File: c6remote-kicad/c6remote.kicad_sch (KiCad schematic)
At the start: 23 parts, among them Q1 MMBT2222A, SW1 SW_Push, SW10 SW_Push, SW11 SW_Push, SW2 SW_Push, SW3 SW_Push, SW4 SW_Push, SW5 SW_Push, SW6 SW_Push, SW7 SW_Push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

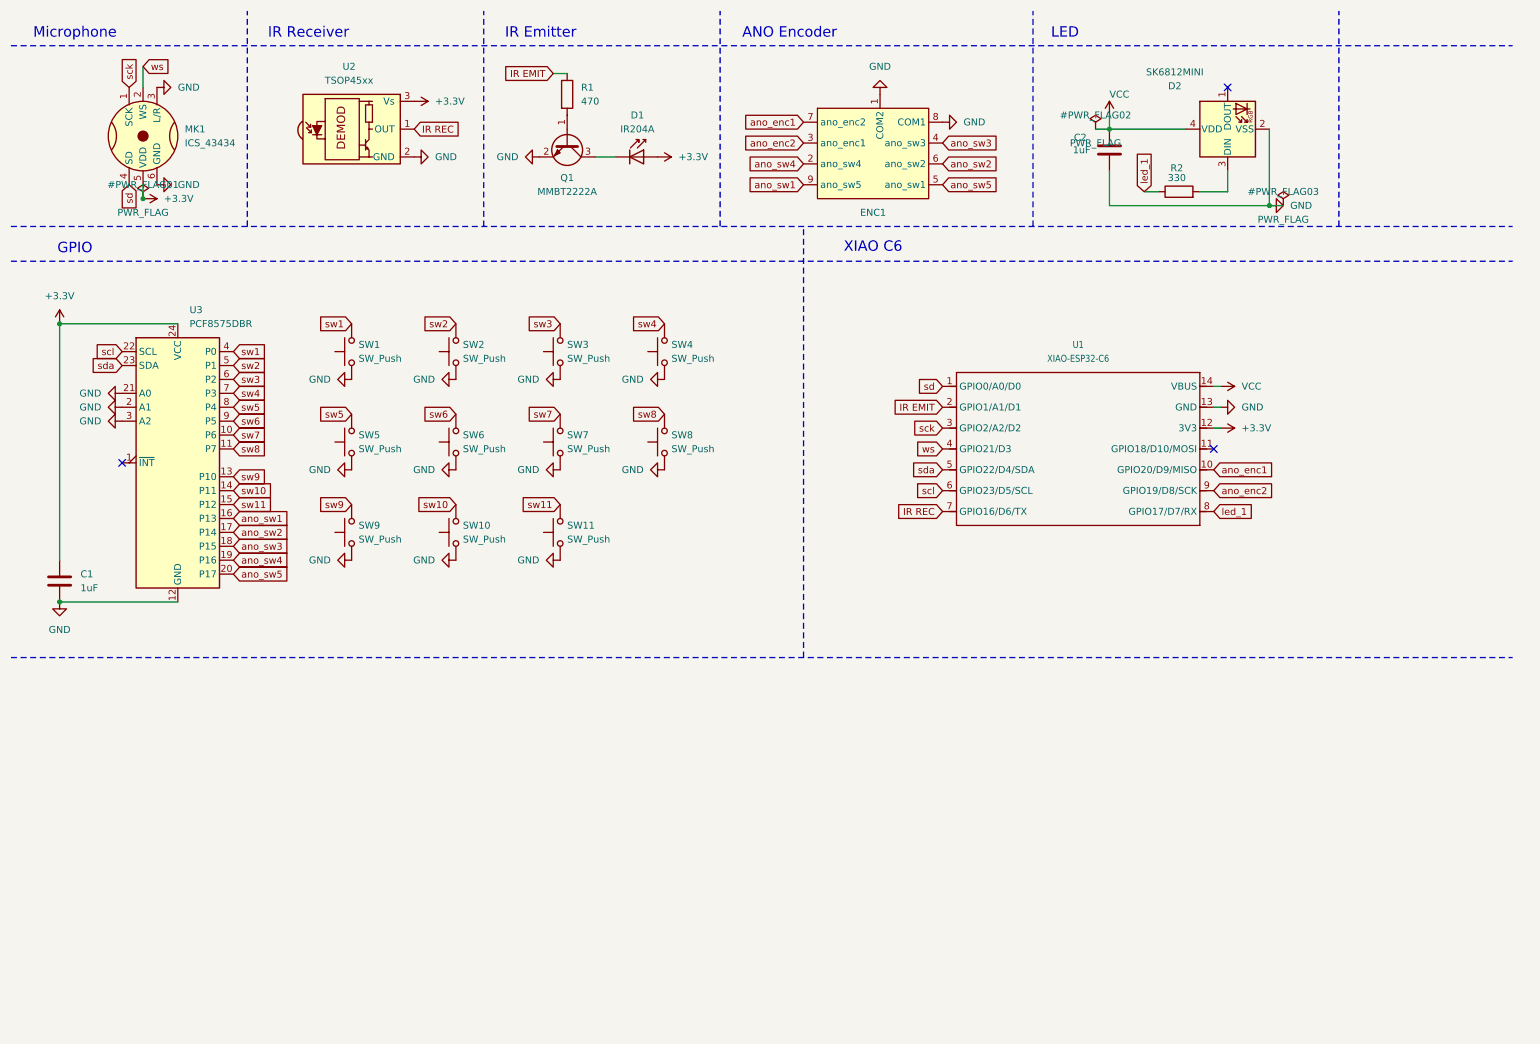
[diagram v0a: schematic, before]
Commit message: feat(kicad): update xiao c6 board
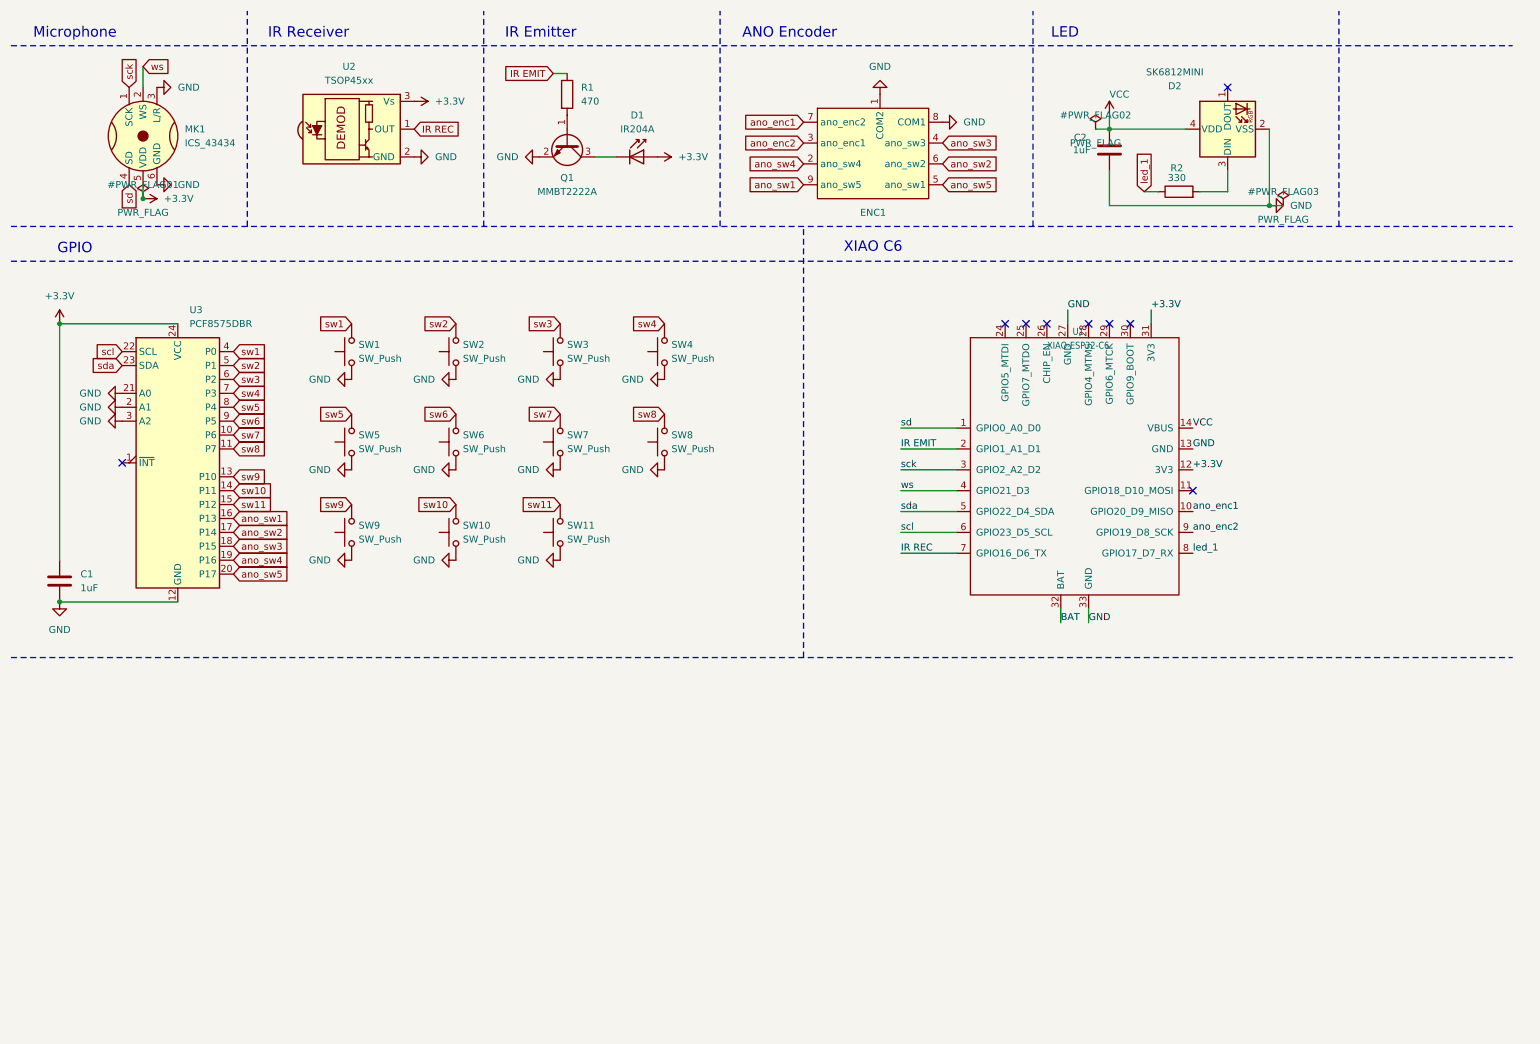
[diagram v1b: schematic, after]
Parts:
- U1: footprint Library:XIAO-ESP32C6-DIP -> Seeed_Studio_XIAO_Series:XIAO-ESP32-C6-SMD; symbol Seeed_Studio_XIAO_Series:XIAO_ESP32-C6-DIP -> Seeed_Studio_XIAO_Series:XIAO-ESP32-C6-SMD
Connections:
- net +3.3V: now also U1.31 (3V3)
- net GND: now also U1.27 (GND), U1.33 (GND)
- new net BAT: U1.32 (BAT)
- no-connect marks 3 -> 9

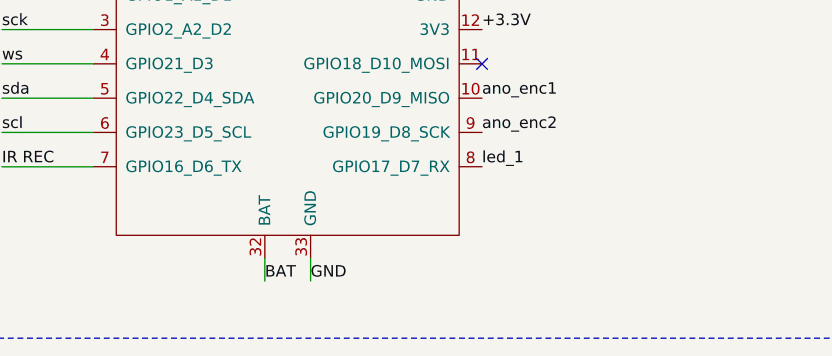
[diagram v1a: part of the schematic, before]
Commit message: fix(kicad): sync battery connector parity
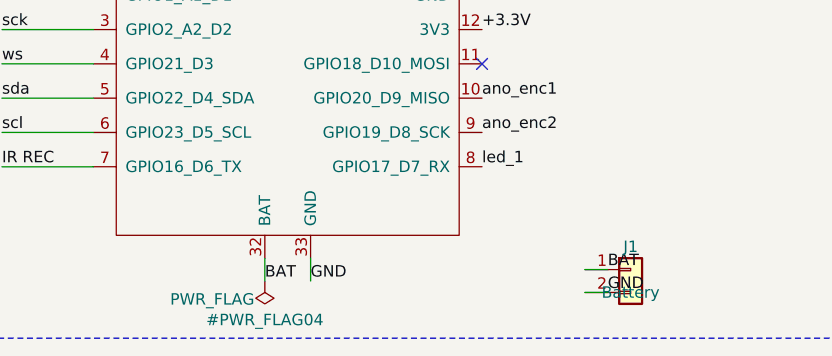
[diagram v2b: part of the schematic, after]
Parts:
- added J1: Battery, Local:WirePad_1x02_P2.54mm_Back, symbol Connector_Generic:Conn_01x02
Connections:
- net BAT: now also J1.1 (Pin_1)
- net GND: now also J1.2 (Pin_2)
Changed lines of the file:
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@@
 	(wire
 		(pts
-			(xy 203.2 120.65) (xy 203.2 123.19)
-		)
-		(stroke
-			(width 0)
-			(type default)
-		)
-	)
-	(wire
-		(pts
 			(xy 212.09 46.99) (xy 241.3 46.99)
 		)
@@
 		)
 	)
+	(wire
+		(pts
+			(xy 238.76 124.46) (xy 241.3 124.46)
+		)
+		(stroke
+			(width 0)
+			(type default)
+		)
+	)
+	(wire
+		(pts
+			(xy 203.2 123.19) (xy 203.2 120.65)
+		)
+		(stroke
+			(width 0)
+			(type default)
+		)
+	)
+	(wire
+		(pts
+			(xy 238.76 121.92) (xy 241.3 121.92)
+		)
+		(stroke
+			(width 0)
+			(type default)
+		)
+	)
 	(polyline
 		(pts
@@
 		)
 	)
-	(label "+3.3V"
-		(at 219.71 66.04 0)
+	(label "GND"
+		(at 241.3 124.46 0)
 		(effects
 			(font
@@
 		)
 	)
-	(label "GND"
-		(at 227.33 91.44 0)
+	(label "+3.3V"
+		(at 219.71 66.04 0)
 		(effects
 			(font
@@
 		)
 	)
-	(label "BAT"
-		(at 203.2 123.19 0)
+	(label "GND"
+		(at 227.33 91.44 0)
 		(effects
 			(font
@@
 		)
 	)
+	(label "BAT"
+		(at 241.3 121.92 0)
+		(effects
+			(font
+				(size 1.27 1.27)
+			)
+			(justify left bottom)
+		)
+	)
 	(label "+3.3V"
 		(at 227.33 95.25 0)
@@
 		)
 	)
+	(label "BAT"
+		(at 203.2 123.19 0)
+		(effects
+			(font
+				(size 1.27 1.27)
+			)
+			(justify left bottom)
+		)
+	)
 	(label "IR EMIT"
 		(at 173.99 91.44 0)
@@
 	)
 	(symbol
+		(lib_id "Connector_Generic:Conn_01x02")
+		(at 243.84 121.92 0)
+		(unit 1)
+		(body_style 1)
+		(exclude_from_sim no)
+		(in_bom yes)
+		(on_board yes)
+		(in_pos_files yes)
+		(dnp no)
+		(property "Reference" "J1"
+			(at 243.84 119.38 0)
+			(show_name no)
+			(do_not_autoplace no)
+			(effects
+				(font
+					(size 1.27 1.27)
+				)
+			)
+		)
+		(property "Value" "Battery"
+			(at 243.84 124.46 0)
+			(show_name no)
+			(do_not_autoplace no)
+			(effects
+				(font
+					(size 1.27 1.27)
+				)
+			)
+		)
+		(property "Footprint" "Local:WirePad_1x02_P2.54mm_Back"
+			(at 243.84 121.92 0)
+			(hide yes)
+			(show_name no)
+			(do_not_autoplace no)
+			(effects
+				(font
+					(size 1.27 1.27)
+				)
+			)
+		)
+		(property "Datasheet" "~"
+			(at 243.84 121.92 0)
+			(hide yes)
+			(show_name no)
+			(do_not_autoplace no)
+			(effects
+				(font
+					(size 1.27 1.27)
+				)
+			)
+		)
+		(property "Description" ""
+			(at 243.84 121.92 0)
+			(show_name no)
+			(do_not_autoplace no)
+			(effects
+				(font
+					(size 1.27 1.27)
+				)
+			)
+		)
+		(pin "1"
+		)
+		(pin "2"
+		)
+		(instances
+			(project "c6remote"
+				(path "/0cbb6fa3-42c1-48e5-afd9-e4923c6691f6"
+					(reference "J1")
+					(unit 1)
+				)
+			)
+		)
+	)
+	(symbol
 		(lib_id "power:GND")
 		(at 241.3 46.99 90)
@@
 					(unit 1)
 				)
+			)
+		)
+	)
+	(symbol
+		(lib_id "power:PWR_FLAG")
+		(at 203.2 123.19 180)
+		(unit 1)
+		(body_style 1)
+		(exclude_from_sim no)
+		(in_bom yes)
+		(on_board yes)
+		(in_pos_files yes)
+		(dnp no)
+		(property "Reference" "#PWR_FLAG04"
+			(at 203.2 127.508 0)
+			(show_name no)
+			(do_not_autoplace no)
+			(effects
+				(font
+					(size 1.27 1.27)
+				)
+			)
+		)
+		(property "Value" "PWR_FLAG"
+			(at 197.358 125.222 0)
+			(show_name no)
+			(do_not_autoplace no)
+			(effects
+				(font
+					(size 1.27 1.27)
+				)
+			)
+		)
+		(property "Footprint" ""
+			(at 203.2 123.19 0)
+			(hide yes)
+			(show_name no)
+			(do_not_autoplace no)
+			(effects
+				(font
+					(size 1.27 1.27)
+				)
+			)
+		)
+		(property "Datasheet" "~"
+			(at 203.2 123.19 0)
+			(hide yes)
+			(show_name no)
+			(do_not_autoplace no)
+			(effects
+				(font
+					(size 1.27 1.27)
+				)
+			)
+		)
+		(property "Description" ""
+			(at 203.2 123.19 0)
+			(show_name no)
+			(do_not_autoplace no)
+			(effects
+				(font
+					(size 1.27 1.27)
+				)
+			)
+		)
+		(pin "1"
+		)
+		(instances
+			(project "c6remote"
+				(path "/0cbb6fa3-42c1-48e5-afd9-e4923c6691f6"
+					(reference "#PWR_FLAG04")
+					(unit 1)
+				)
